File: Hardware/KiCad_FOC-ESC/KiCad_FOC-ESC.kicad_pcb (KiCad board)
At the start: 6 copper layers, 51 x 46 mm, 70 parts, among them IC1 TCAN3414DDFR, IC2 TSC1801BILT, IC3 TSC1801BILT, IC4 TSC1801BILT, IC5 REF2030AIDDCR, IC6 MA702GQ-P, IC901 DRV8320SRTVR, J1 Conn_01x06, J2 Prog, Q1 NTTFS5D6N08XLTAG, Q2 NTTFS5D6N08XLTAG, Q3 NTTFS5D6N08XLTAG, Q4 NTTFS5D6N08XLTAG, Q5 NTTFS5D6N08XLTAG, Q6 NTTFS5D6N08XLTAG, U1 STM32G473RCTx, U3 MT6701CT, U802 ZLDO1117Q, Y1 ASDDV-16.000MHZ-LR-T

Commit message: layouted prog. pins (#21)
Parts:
- R1: footprint Resistor_SMD:R_0603_1608Metric -> Resistor_SMD:R_0402_1005Metric
- moved C18 19.8 mm to (109.0, 82.0), turned to 90 degrees
- moved R1 15.8 mm to (108.0, 82.0), turned to 90 degrees
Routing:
- net VCC: track 10.6 -> 35.0 mm
- net +3V3: track 162.9 -> 169.9 mm, vias 14 -> 15
- net NRST: track 17.2 -> 20.5 mm
- net GND: track 35.8 -> 36.8 mm, vias 119 -> 120
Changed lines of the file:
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@@
 		)
 		(pad "1" smd roundrect
-			(at -2.575 -1.905 180)
-			(size 1.75 0.6)
+			(at -2.874311 -1.907092 180)
+			(size 1.151346 0.595794)
 			(layers "F.Cu" "F.Mask" "F.Paste")
 			(roundrect_rratio 0.25)
@@
 		)
 		(pad "2" smd roundrect
-			(at -2.575 -0.635 180)
-			(size 1.75 0.6)
+			(at -2.87499 -0.635 180)
+			(size 1.14998 0.6)
 			(layers "F.Cu" "F.Mask" "F.Paste")
 			(roundrect_rratio 0.25)
@@
 		)
 		(pad "3" smd roundrect
-			(at -2.575 0.635 180)
-			(size 1.75 0.6)
+			(at -2.874991 0.634991 180)
+			(size 1.149982 0.599982)
 			(layers "F.Cu" "F.Mask" "F.Paste")
 			(roundrect_rratio 0.25)
@@
 		)
 		(pad "4" smd roundrect
-			(at -2.575 1.905 180)
-			(size 1.75 0.6)
+			(at -2.874994 1.904993 180)
+			(size 1.149988 0.599986)
 			(layers "F.Cu" "F.Mask" "F.Paste")
 			(roundrect_rratio 0.25)
@@
 		)
 		(pad "5" smd roundrect
-			(at 2.575 1.905 180)
-			(size 1.75 0.6)
+			(at 2.879341 1.897268 180)
+			(size 1.141298 0.615444)
 			(layers "F.Cu" "F.Mask" "F.Paste")
 			(roundrect_rratio 0.25)
@@
 		)
 		(pad "6" smd roundrect
-			(at 2.575 0.635 180)
-			(size 1.75 0.6)
+			(at 2.874996 0.634998 180)
+			(size 1.149992 0.599996)
 			(layers "F.Cu" "F.Mask" "F.Paste")
 			(roundrect_rratio 0.25)
@@
 		)
 		(pad "7" smd roundrect
-			(at 2.575 -0.635 180)
-			(size 1.75 0.6)
+			(at 2.872731 -0.630573 180)
+			(size 1.154528 0.591146)
 			(layers "F.Cu" "F.Mask" "F.Paste")
 			(roundrect_rratio 0.25)
@@
 		)
 		(pad "8" smd roundrect
-			(at 2.575 -1.905 180)
-			(size 1.75 0.6)
+			(at 2.87505 -1.9061 180)
+			(size 1.149862 0.597748)
 			(layers "F.Cu" "F.Mask" "F.Paste")
 			(roundrect_rratio 0.25)
@@
 		(embedded_fonts no)
 	)
-	(footprint "Resistor_SMD:R_0603_1608Metric"
+	(footprint "Resistor_SMD:R_0402_1005Metric"
 		(layer "F.Cu")
-		(at 102.405 67.255)
-		(descr "Resistor SMD 0603 (1608 Metric), square (rectangular) end terminal, IPC-7351 nominal, (Body size source: IPC-SM-782 page 72, https://www.pcb-3d.com/wordpress/wp-content/uploads/ipc-sm-782a_amendment_1_and_2.pdf)")
+		(at 108.03 82.01 90)
+		(descr "Resistor SMD 0402 (1005 Metric), square (rectangular) end terminal, IPC-7351 nominal, (Body size source: IPC-SM-782 page 72, https://www.pcb-3d.com/wordpress/wp-content/uploads/ipc-sm-782a_amendment_1_and_2.pdf)")
 		(tags "resistor")
 		(property "Reference" "R1"
-			(at 0 -1.43 0)
+			(at 0 -1.17 90)
 			(layer "F.SilkS")
 			(hide yes)
@@
 		)
 		(property "Value" "10k"
-			(at 0 1.43 0)
+			(at 0 -1 90)
 			(layer "F.SilkS")
 			(effects
 				(font
-					(size 1 1)
+					(size 0.75 0.75)
 					(thickness 0.15)
 				)
@@
 		)
 		(property "Datasheet" ""
-			(at 0 0 0)
+			(at 0 0 90)
 			(layer "F.Fab")
 			(hide yes)
@@
 		)
 		(property "Description" "Resistor"
-			(at 0 0 0)
+			(at 0 0 90)
 			(layer "F.Fab")
 			(hide yes)
@@
 		)
 		(property "KiLib_Generator" "SMD_2terminal_chip_molded"
-			(at 0 0 0)
+			(at 0 0 90)
 			(layer "F.SilkS")
 			(hide yes)
@@
 		(duplicate_pad_numbers_are_jumpers no)
 		(fp_line
-			(start -0.237258 -0.5225)
-			(end 0.237258 -0.5225)
+			(start -0.153641 -0.38)
+			(end 0.153641 -0.38)
 			(stroke
 				(width 0.12)
@@
 		)
 		(fp_line
-			(start -0.237258 0.5225)
-			(end 0.237258 0.5225)
+			(start -0.153641 0.38)
+			(end 0.153641 0.38)
 			(stroke
 				(width 0.12)
@@
 		)
 		(fp_rect
-			(start -1.48 -0.73)
-			(end 1.48 0.73)
+			(start -0.93 -0.47)
+			(end 0.93 0.47)
 			(stroke
 				(width 0.05)
@@
 		)
 		(fp_rect
-			(start -0.8 -0.4125)
-			(end 0.8 0.4125)
+			(start -0.525 -0.27)
+			(end 0.525 0.27)
 			(stroke
 				(width 0.1)
@@
 		)
 		(fp_text user "${REFERENCE}"
-			(at 0 0 0)
+			(at 0 0 90)
 			(layer "F.Fab")
 			(effects
 				(font
-					(size 0.4 0.4)
-					(thickness 0.06)
+					(size 0.26 0.26)
+					(thickness 0.04)
 				)
 			)
 		)
 		(pad "1" smd roundrect
-			(at -0.825 0)
-			(size 0.8 0.95)
+			(at -0.51 0 90)
+			(size 0.54 0.64)
 			(layers "F.Cu" "F.Mask" "F.Paste")
 			(roundrect_rratio 0.25)
@@
 		)
 		(pad "2" smd roundrect
-			(at 0.825 0)
-			(size 0.8 0.95)
+			(at 0.51 0 90)
+			(size 0.54 0.64)
 			(layers "F.Cu" "F.Mask" "F.Paste")
 			(roundrect_rratio 0.25)
@@
 		)
 		(embedded_fonts no)
-		(model "${KICAD10_3DMODEL_DIR}/Resistor_SMD.3dshapes/R_0603_1608Metric.step"
+		(model "${KICAD10_3DMODEL_DIR}/Resistor_SMD.3dshapes/R_0402_1005Metric.step"
 			(offset
 				(xyz 0 0 0)
@@
 	(footprint "Capacitor_SMD:C_0402_1005Metric"
 		(layer "F.Cu")
-		(at 96.8 66.4)
+		(at 109.03 82.01 90)
 		(descr "Capacitor SMD 0402 (1005 Metric), square (rectangular) end terminal, IPC-7351 nominal, (Body size source: IPC-SM-782 page 76, https://www.pcb-3d.com/wordpress/wp-content/uploads/ipc-sm-782a_amendment_1_and_2.pdf)")
 		(tags "capacitor")
 		(property "Reference" "C18"
-			(at 0 -1.16 0)
+			(at 0 -1.16 90)
 			(layer "F.SilkS")
 			(hide yes)
@@
 		)
 		(property "Value" "100nF"
-			(at 0 1.16 0)
+			(at 0 1.16 90)
 			(layer "F.SilkS")
 			(effects
 				(font
-					(size 1 1)
+					(size 0.75 0.75)
 					(thickness 0.15)
 				)
@@
 		)
 		(property "Datasheet" ""
-			(at 0 0 0)
+			(at 0 0 90)
 			(layer "F.Fab")
 			(hide yes)
@@
 		)
 		(property "Description" "Unpolarized capacitor"
-			(at 0 0 0)
+			(at 0 0 90)
 			(layer "F.Fab")
 			(hide yes)
@@
 		)
 		(property "KiLib_Generator" "SMD_2terminal_chip_molded"
-			(at 0 0 0)
+			(at 0 0 90)
 			(layer "F.SilkS")
 			(hide yes)
@@
 		)
 		(fp_text user "${REFERENCE}"
-			(at 0 0 0)
+			(at 0 0 90)
 			(layer "F.Fab")
 			(effects
@@
 		)
 		(pad "1" smd roundrect
-			(at -0.48 0)
+			(at -0.48 0 90)
 			(size 0.56 0.62)
 			(layers "F.Cu" "F.Mask" "F.Paste")
@@
 		)
 		(pad "2" smd roundrect
-			(at 0.48 0)
+			(at 0.48 0 90)
 			(size 0.56 0.62)
 			(layers "F.Cu" "F.Mask" "F.Paste")
@@
 	)
 	(segment
+		(start 108.03 83.5)
+		(end 108.03 82.52)
+		(width 0.2)
+		(layer "F.Cu")
+		(net "+3V3")
+	)
+	(segment
 		(start 130.15682 63.451447)
 		(end 129.805992 63.802274)
@@
 	)
 	(via
+		(at 108.03 83.5)
+		(size 0.6)
+		(drill 0.3)
+		(layers "F.Cu" "B.Cu")
+		(net "+3V3")
+	)
+	(via
 		(at 123.135 91.389711)
 		(size 0.4)
@@
 	)
 	(segment
+		(start 108.5 85)
+		(end 110.5 85)
+		(width 0.25)
+		(layer "In2.Cu")
+		(net "+3V3")
+	)
+	(segment
 		(start 112.535 84.298553)
 		(end 117.2 79.633553)
@@
 	)
 	(segment
+		(start 108 84.5)
+		(end 108.5 85)
+		(width 0.25)
+		(layer "In2.Cu")
+		(net "+3V3")
+	)
+	(segment
+		(start 112.535 84.5)
+		(end 112.535 84.298553)
+		(width 0.25)
+		(layer "In2.Cu")
+		(net "+3V3")
+	)
+	(segment
 		(start 135.2 81.8)
 		(end 135.200001 81.799999)
@@
 	)
 	(segment
+		(start 110.5 85)
+		(end 111.201447 84.298553)
+		(width 0.25)
+		(layer "In2.Cu")
+		(net "+3V3")
+	)
+	(segment
 		(start 125.234923 79.017514)
 		(end 125.217514 79.017514)
@@
 	)
 	(segment
+		(start 108 83.53)
+		(end 108 84.5)
+		(width 0.25)
+		(layer "In2.Cu")
+		(net "+3V3")
+	)
+	(segment
+		(start 108.03 83.5)
+		(end 108 83.53)
+		(width 0.25)
+		(layer "In2.Cu")
+		(net "+3V3")
+	)
+	(segment
+		(start 111.201447 84.298553)
+		(end 112.535 84.298553)
+		(width 0.25)
+		(layer "In2.Cu")
+		(net "+3V3")
+	)
+	(segment
 		(start 117.2 76.356602)
 		(end 115.688982 74.845584)
@@
 	(segment
 		(start 112.535 91.389711)
-		(end 112.535 84.298553)
+		(end 112.535 84.5)
 		(width 0.25)
 		(layer "In2.Cu")
@@
 	)
 	(segment
+		(start 109.03 83.5)
+		(end 109.03 82.49)
+		(width 0.2)
+		(layer "F.Cu")
+		(net "GND")
+	)
+	(segment
 		(start 115.445404 78.658579)
 		(end 115.460378 78.673553)
@@
 	)
 	(via
+		(at 109.03 83.5)
+		(size 0.6)
+		(drill 0.3)
+		(layers "F.Cu" "B.Cu")
+		(net "GND")
+	)
+	(via
 		(at 139.51767 73.211649)
 		(size 0.4)
@@
 	)
 	(segment
+		(start 109.03 80.845064)
+		(end 109.03 81.53)
+		(width 0.2)
+		(layer "F.Cu")
+		(net "NRST")
+	)
+	(segment
+		(start 108.03 81.5)
+		(end 109 81.5)
+		(width 0.2)
+		(layer "F.Cu")
+		(net "NRST")
+	)
+	(segment
 		(start 118.1 69.782233)
 		(end 116.872917 69.782233)
@@
 		(net "NRST")
 	)
+	(segment
+		(start 109 81.5)
+		(end 109.03 81.53)
+		(width 0.2)
+		(layer "F.Cu")
+		(net "NRST")
+	)
+	(segment
+		(start 107.85 79.665064)
+		(end 109.03 80.845064)
+		(width 0.2)
+		(layer "F.Cu")
+		(net "NRST")
+	)
 	(via
 		(at 107.85 79.665064)
@@
 	)
 	(segment
+		(start 136.774997 86.125003)
+		(end 131.4 91.5)
+		(width 0.3)
+		(layer "B.Cu")
+		(net "VCC")
+	)
+	(segment
 		(start 136.149995 80.474998)
 		(end 136.774997 81.1)
@@
 		(width 0.3)
 		(layer "B.Cu")
+		(net "VCC")
+	)
+	(segment
+		(start 131.4 91.5)
+		(end 131.4 103.3)
+		(width 0.3)
+		(layer "B.Cu")
+		(net "VCC")
+	)
+	(segment
+		(start 136.774997 81.1)
+		(end 136.774997 86.125003)
+		(width 0.3)
+		(layer "B.Cu")

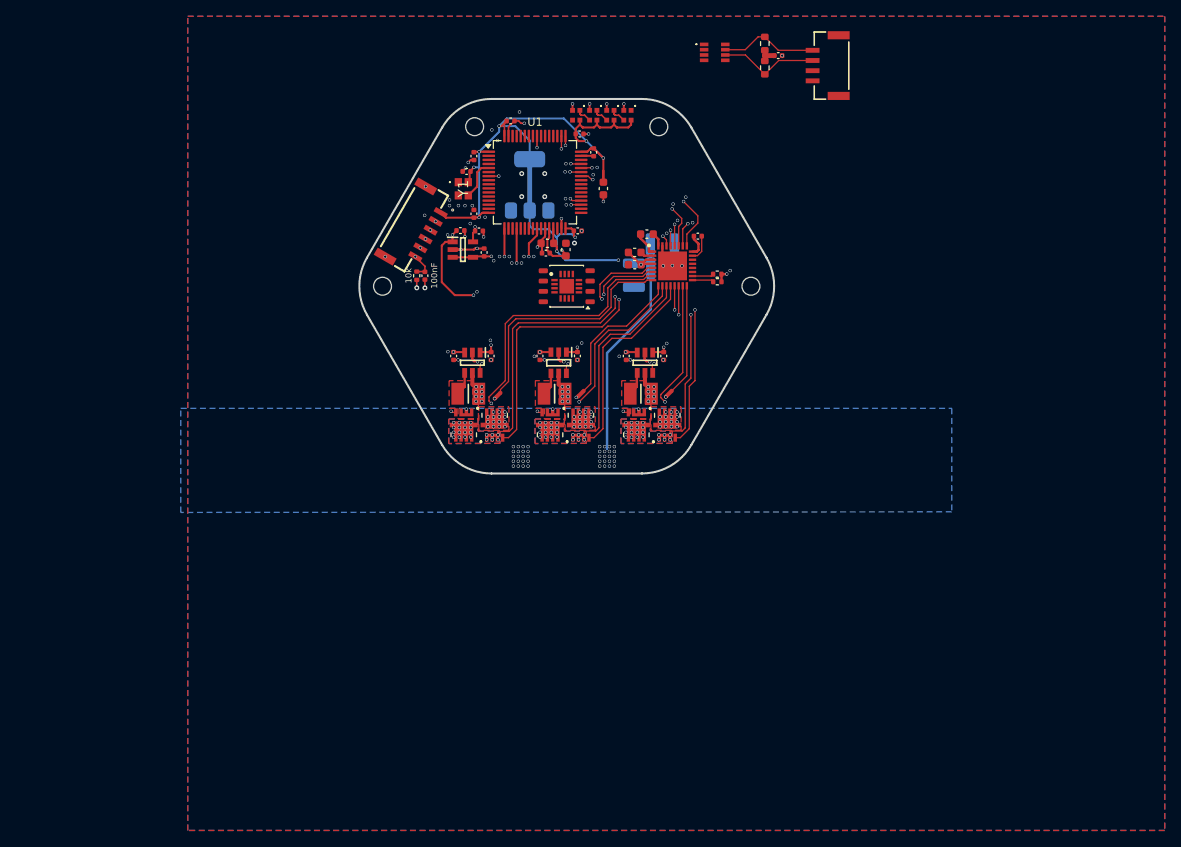
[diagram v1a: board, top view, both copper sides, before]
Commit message: Foc esc/stm32 idefo cinit (#22)
* edited FOC-ESC connections

* added CAN
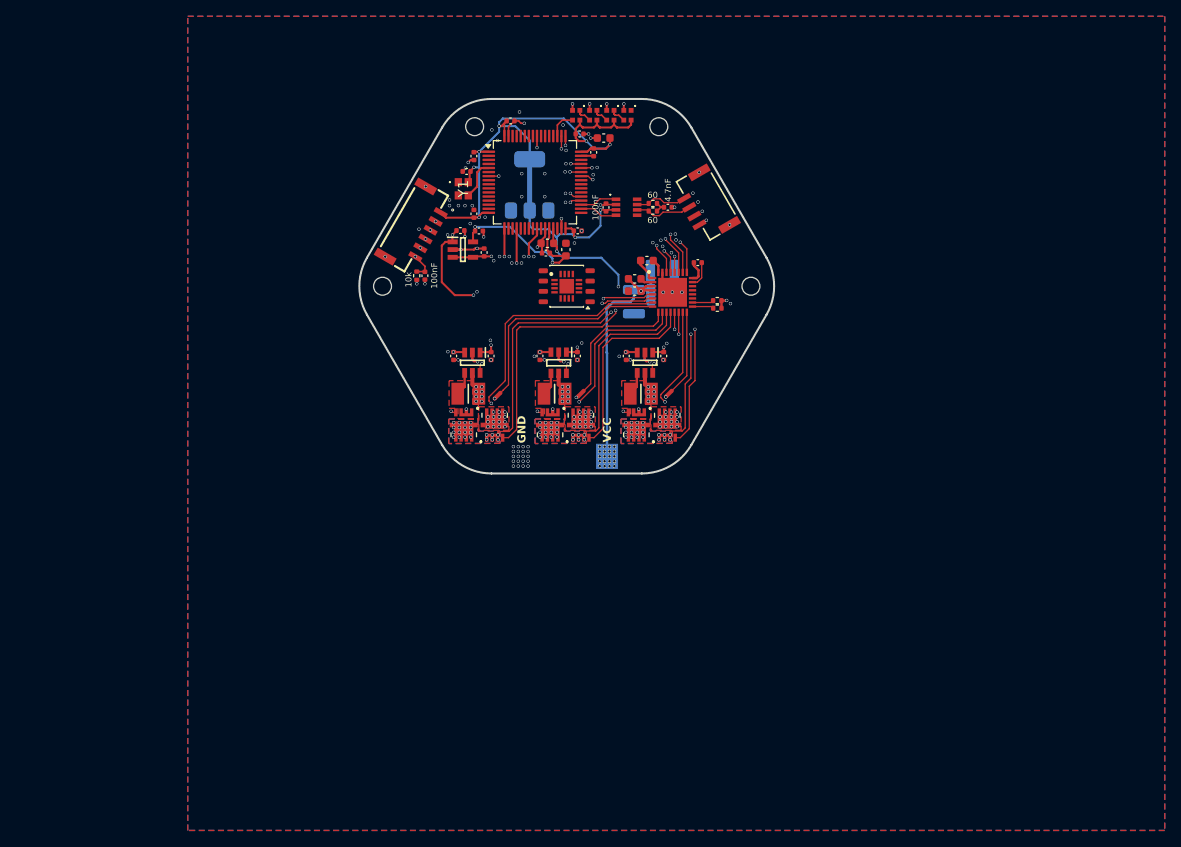
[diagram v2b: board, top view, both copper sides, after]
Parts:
- added C22: 100nF, Capacitor_SMD:C_0402_1005Metric, F.Cu at (131.3, 73.6)
- R2, R3: footprint Resistor_SMD:R_0603_1608Metric -> Resistor_SMD:R_0402_1005Metric
- moved R2 24.0 mm to (137.0, 73.1), turned to 0 degrees
- moved J1 23.2 mm to (142.0, 74.0), turned to 120 degrees
- moved C21 23.0 mm to (138.9, 73.6)
- moved R3 22.3 mm to (137.0, 74.1), turned to 180 degrees
- moved IC1 21.9 mm to (133.8, 73.6)
- moved C1 6.20 mm to (131.0, 65.1), turned to 180 degrees
- moved C110 3.25 mm to (138.2, 84.4)
- moved C116 3.25 mm to (138.2, 81.4)
- moved C901 3.25 mm to (142.6, 80.4)
- moved C902 3.25 mm to (134.8, 82.4)
- moved C903 3.25 mm to (134.8, 83.9)
- moved C904 3.25 mm to (136.3, 80.2)
- moved C122 3.25 mm to (134.7, 85.2)
- moved IC901 3.25 mm to (139.4, 84.0)
- moved R901 3.25 mm to (144.9, 85.1)
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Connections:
- net CANH renamed CAN+
- net CANL renamed CAN-
- J1 pad 1: unconnected-(J1-Pin_1-Pad1) -> +3V3
- U1 pad 34: unconnected-(U1-PB12-Pad34) -> CANRX
- U1 pad 35: INLC -> CANTX
- U1 pad 37: unconnected-(U1-PB15-Pad37) -> INLC
- U1 pad 51: unconnected-(U1-PA15-Pad51) -> DebugLED_IN
- U1 pad 57: CAN_STB -> unconnected-(U1-PB4-Pad57)
- U1 pad 58: CAN_SHDNVIO -> unconnected-(U1-PB5-Pad58)
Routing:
- net +3V3: track 169.9 -> 187.8 mm, vias 15 -> 17
- net +3V: track 8.28 -> 21.1 mm
- net INLC: track 16.0 -> 21.8 mm
- net CAN+: track 12.2 -> 6.49 mm
- net CAN-: track 12.4 -> 7.12 mm
- net CANRX: track 0.00 -> 4.67 mm
- net CANTX: track 0.00 -> 4.59 mm
- net GHA: track 40.7 -> 36.2 mm
- net INLB: track 18.6 -> 22.3 mm
- net DebugLED_IN: track 0.00 -> 3.47 mm
- net SHA: track 38.8 -> 35.4 mm
- net GLC: track 22.1 -> 18.8 mm
- net GHC: track 22.5 -> 19.3 mm
- net /FETs/DRV8320S_1/SPC: track 13.7 -> 10.4 mm
- net SHC: track 21.6 -> 18.5 mm
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- removed copper zone on B.Cu, net VCC
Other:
- board text added: "A"
- board text added: "B"
- board text added: "C"
- board text added: "GND"
- board text added: "VCC"
- board text added: "add humongous Caps."

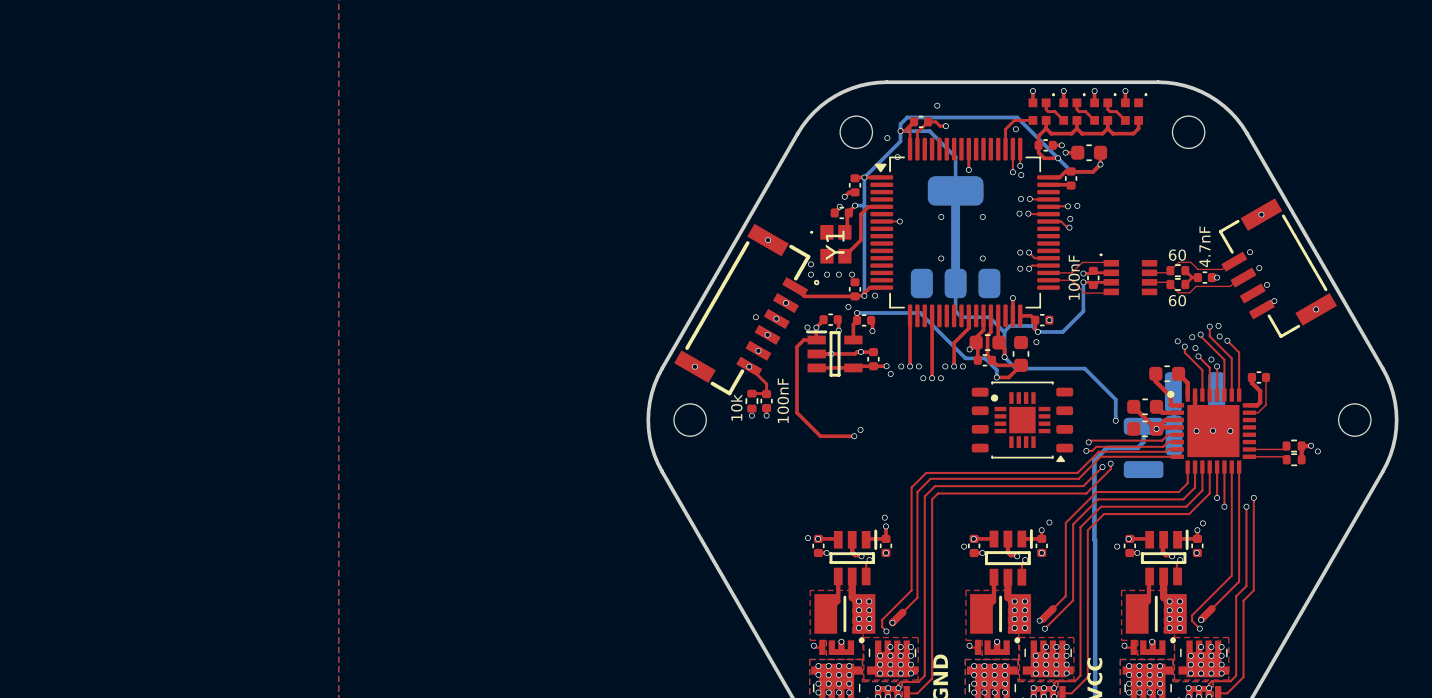
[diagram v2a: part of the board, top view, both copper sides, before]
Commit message: added:USB, edited:CAN
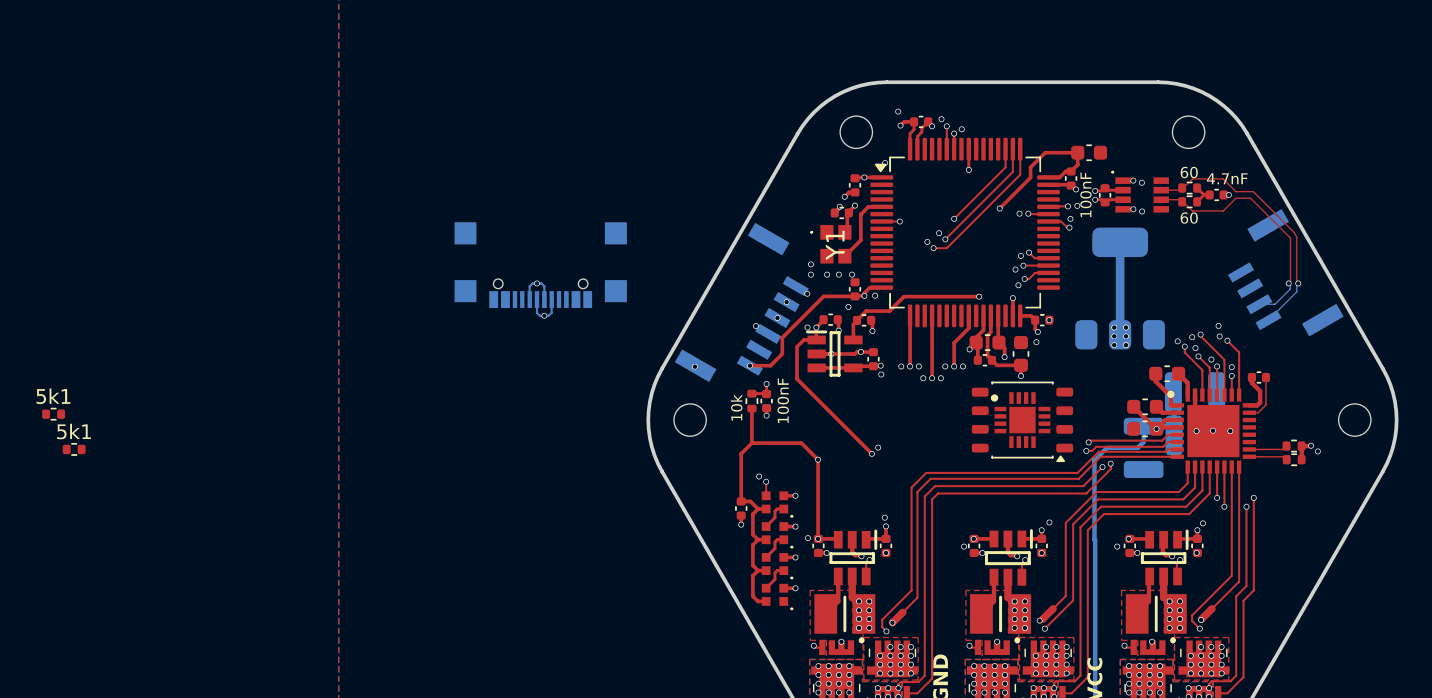
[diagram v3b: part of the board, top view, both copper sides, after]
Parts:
- added J201: GSB1C41110SSHR, SamacSys_Parts:GSB1C41110SSHR, B.Cu at (93.7, 71.7)
- added R7: 5k1, Resistor_SMD:R_0402_1005Metric, F.Cu at (61.9, 85.3)
- added R8: 5k1, Resistor_SMD:R_0402_1005Metric, F.Cu at (60.5, 82.9)
- J1, J2: moved to B.Cu
- moved D4 40.9 mm to (109.6, 95.2), turned to 0 degrees
- moved D3 38.0 mm to (109.6, 93.1), turned to 0 degrees
- moved D2 35.0 mm to (109.6, 91.0), turned to 0 degrees
- moved C7 32.3 mm to (107.3, 89.3), turned to -90 degrees
- moved D1 32.1 mm to (109.6, 88.9), turned to 0 degrees
- moved U802 11.7 mm to (133.1, 74.3)
- moved J2 10.7 mm to (103.0, 79.4), turned to 60 degrees
- moved R2 5.68 mm to (137.8, 67.5)
- moved R3 5.68 mm to (137.8, 68.4)
- moved C21 5.68 mm to (139.7, 68.0)
- moved C22 5.68 mm to (132.1, 68.0)
- moved IC1 5.68 mm to (134.6, 68.0)
- moved J1 0.86 mm to (142.4, 74.8), turned to -60 degrees
- turned C1 to 0 degrees
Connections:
- U1 pad 34: CANRX -> unconnected-(U1-PB12-Pad34)
- U1 pad 35: CANTX -> INLA
- U1 pad 45: INLA -> USB-
- U1 pad 46: unconnected-(U1-PA12-Pad46) -> USB+
- U1 pad 58: unconnected-(U1-PB5-Pad58) -> CANRX
- U1 pad 59: unconnected-(U1-PB6-Pad59) -> CANTX
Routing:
- net DebugLED_IN: track 3.47 -> 32.8 mm, vias 0 -> 2
- net CANTX: track 4.59 -> 16.7 mm, vias 0 -> 2
- net CANRX: track 4.67 -> 16.1 mm, vias 0 -> 2
- net CAN+: track 6.49 -> 17.6 mm, vias 0 -> 1
- net CAN-: track 7.12 -> 16.5 mm, vias 0 -> 1
- net +3V3: track 187.8 -> 181.3 mm, vias 17 -> 21
- net SWO: track 23.6 -> 20.3 mm
- net +3V: track 21.1 -> 24.3 mm
- net USB+: track 0.00 -> 2.97 mm, vias 0 -> 1
- net USB-: track 0.00 -> 2.97 mm, vias 0 -> 1
- net SWCLK: track 25.0 -> 22.3 mm
- net GND: track 38.7 -> 37.0 mm, vias 129 -> 122
- net SWDIO: track 24.5 -> 26.0 mm
- net +1V5: track 57.4 -> 56.1 mm
- net INLA: track 24.1 -> 23.1 mm
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- added copper zone on In2.Cu, net +3V3
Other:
- board text added: "add humongous Caps. ferrat beat bei VDDA Abstand von CAN leitung zwischen den differenziellen pair"
- board text removed: "add humongous Caps."
